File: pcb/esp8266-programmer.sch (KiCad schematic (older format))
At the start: 20 parts, among them P1 USB_OTG, P2 CONN_01X04, P3 CONN_01X05, P4 CONN_01X05, SW1 RESET, SW2 FLASH, SW3 SW_DP3T, U1 MCP1700T-3302E/TT, U2 MCP2221-I/SL, U3 74LS125, U99 ESP-12

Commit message: Interim stage
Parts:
- removed P1: USB_OTG, symbol USB_OTG-RESCUE-esp8266-programmer
- removed P3, P4: CONN_01X05, symbol CONN_01X05
- removed U3: 74LS125, symbol 74LS125
- added P1: USB_OTG, ruriwo/KiCad_MicroUSB.pretty:ZX62R-B-5P, symbol USB_OTG
- added P3: CONN_02X05, madworm/DIL-Headers.pretty:DIL-5, symbol CONN_02X05
- added R5: 10K, KiCad/Resistors_SMD.pretty:R_1206_HandSoldering, symbol R
- C1, C2, C3: footprint (none) -> KiCad/Capacitors_ThroughHole.pretty:CP_Radial_D5.0mm_P2.50mm
- C4: footprint (none) -> KiCad/Capacitors_SMD.pretty:C_1206_HandSoldering
- JP1: footprint (none) -> madworm/SIL-Headers.pretty:SIL-3
- P2: footprint (none) -> madworm/SIL-Headers.pretty:SIL-5
- R1, R2, R3, R4: value R -> 10K; footprint (none) -> KiCad/Resistors_SMD.pretty:R_1206_HandSoldering
- SW1, SW2: footprint (none) -> KiCad/Buttons_Switches_ThroughHole.pretty:SW_PUSH_6mm_h4.3mm
- SW3: footprint (none) -> KiCad/Buttons_Switches_ThroughHole.pretty:SW_DIP_x3_W7.62mm_Slide_LowProfile
- U2: footprint IPC7351-Nominal:SOIC127P600X175-14 -> KiCad/Housings_SOIC.pretty:SOIC-14_3.9x8.7mm_Pitch1.27mm
- U99: footprint jdunmire/kicad-ESP8266/ESP8266.pretty:ESP-12 -> bgowland/esp12-pogo_pins:ESP-12-with-pogo-pin-pads
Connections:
- net D+: now also P1.3 (D+)
- net D-: now also P1.2 (D-)
- net GND: now also P1.5 (GND), P1.6 (shield), R5.2; no longer C2.1, C3.1, R1.1, R2.1, R3.1, R4.1, SW3.1, SW3.6 (ComB), U2.1 (V+), U99.10 (GPIO15), U99.8 (VCC)
- net PP_ADC: now also P3.1 (P1)
- net PP_GPIO0: now also P3.6 (P6)
- net PP_GPIO12: now also P3.7 (P7)
- net PP_GPIO13: now also P3.9 (P9)
- net PP_GPIO14: now also P3.5 (P5)
- net PP_GPIO16: now also P3.3 (P3)
- net PP_GPIO2: now also P3.8 (P8)
- net PP_GPIO4: now also P3.4 (P4)
- net PP_GPIO5: now also P3.2 (P2)
- new net PP_GPIO15: P3.10 (P10), R5.1, U99.10 (GPIO15)
- new net VBUS: C3.1, P1.1 (VBUS), SW3.1, U2.1 (V+)
- new net VCC: C2.1, R1.1, R2.1, R3.1, R4.1, SW3.6 (ComB), U99.8 (VCC)
- no-connect marks 8 -> 11
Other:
- moved on the sheet: C3, R2

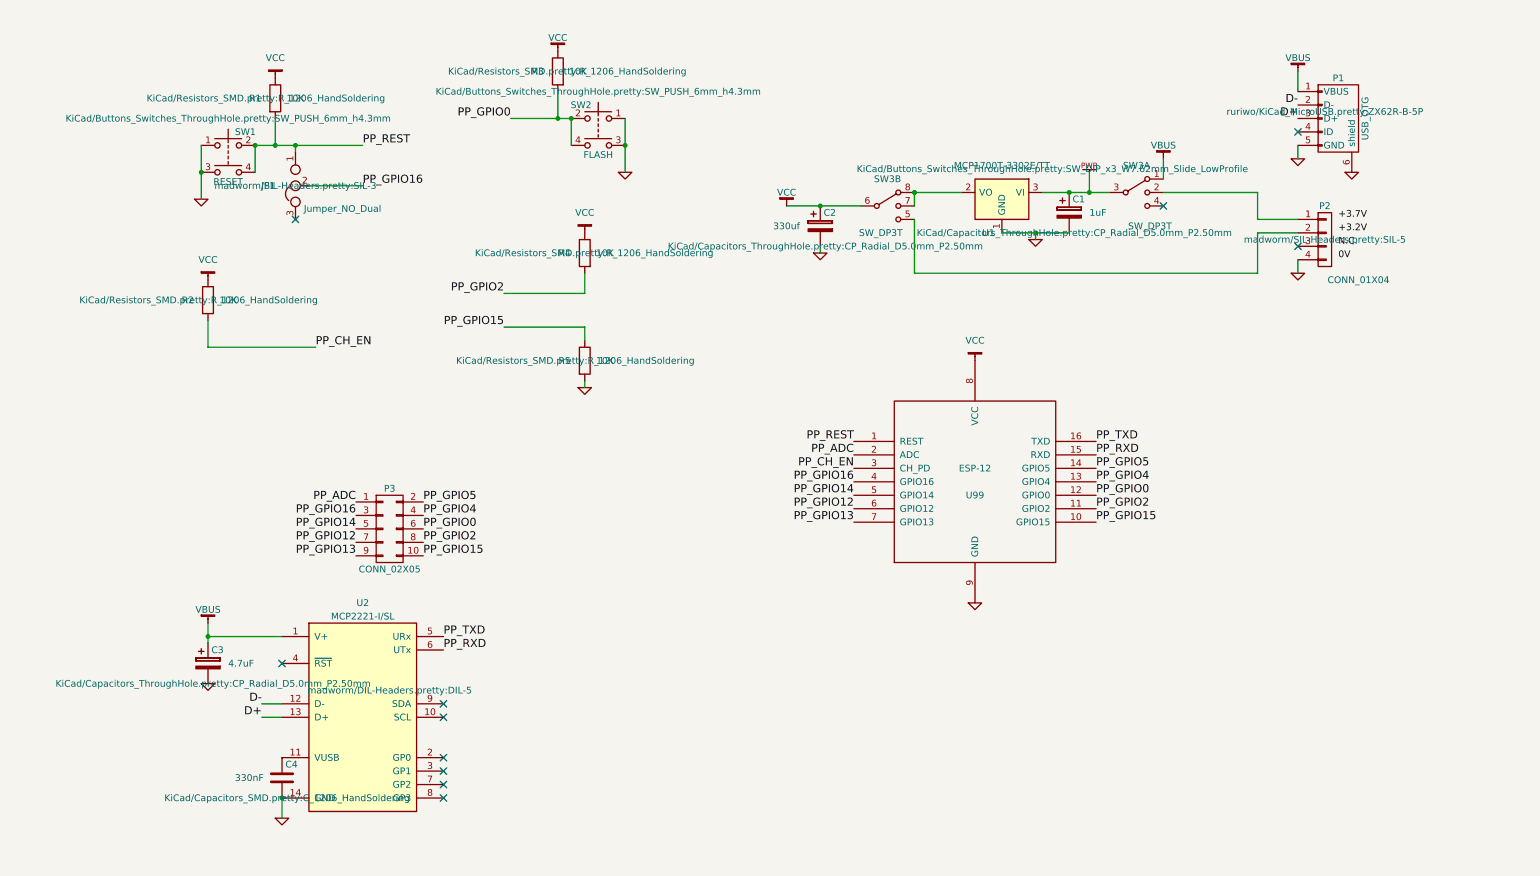
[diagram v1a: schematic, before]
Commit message: Add CH340G and new reset/flash circuit
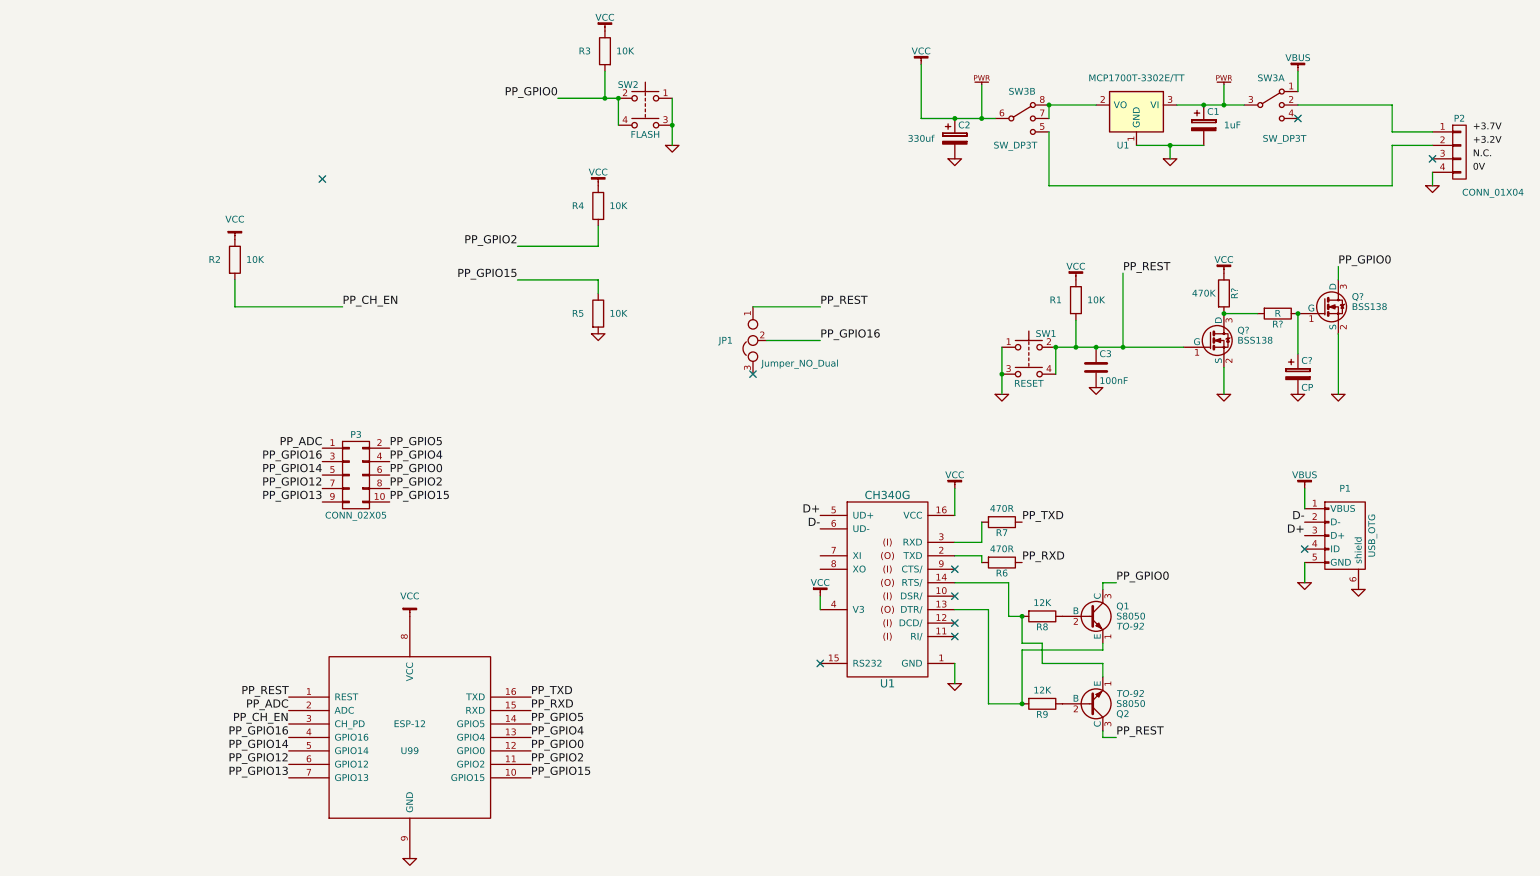
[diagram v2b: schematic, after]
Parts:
- removed C3: 4.7uF, KiCad/Capacitors_ThroughHole.pretty:CP_Radial_D5.0mm_P2.50mm, symbol CP
- removed C4: 330nF, KiCad/Capacitors_SMD.pretty:C_1206_HandSoldering, symbol C
- removed U2: MCP2221-I/SL, KiCad/Housings_SOIC.pretty:SOIC-14_3.9x8.7mm_Pitch1.27mm, symbol MCP2221-I/SL
- added C3: 100nF, symbol C
- added C?: CP, symbol CP
- added Q1, Q2: S8050, TO-92, symbol S8050
- added Q? (x2): BSS138, TO_SOT_Packages_SMD:SOT-23, symbol BSS138
- added R6, R7: 470R, symbol R
- added R8, R9: 12K, symbol R
- added R?: 470K, symbol R
- added R?: R, symbol R
- added U1: CH340G, symbol CH340G
- P1: footprint ruriwo/KiCad_MicroUSB.pretty:ZX62R-B-5P -> greatscottgadgets/gsg-kicad-lib/gsg-modules.pretty:USB-MICROB-FCI-10103592-LONGPADS
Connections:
- net D+: now also U1.5 (UD+)
- net D-: now also U1.6 (UD-)
- net GND: now also C3.2, C?.2, Q?.2 (S), Q?.2 (S), U1.1 (GND)
- net PP_GPIO0: now also Q1.3 (C), Q?.3 (D)
- net PP_REST: now also C3.1, Q2.3 (C), Q?.1 (G)
- net PP_RXD: now also R6.1
- net PP_TXD: now also R7.1
- net VCC: now also R?.1, U1.16 (VCC), U1.4 (V3)
- new net: Q1.1 (E), R9.2, U1.13 (DTR/)
- new net: Q2.1 (E), R8.2, U1.14 (RTS/)
- new net: R6.2, U1.2 (TXD)
- new net: R7.2, U1.3 (RXD)
- new net: Q1.2 (B), R8.1
- new net: Q2.2 (B), R9.1
- new net: C?.1, Q?.1 (G), R?.1
- new net: Q?.3 (D), R?.2, R?.2
- no-connect marks 11 -> 10
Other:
- moved on the sheet: C1, C2, JP1, P2, P3, R1, R2, R3, R4, R5, SW1, SW2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

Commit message: Add final components for CH230G & RST/FLA switch
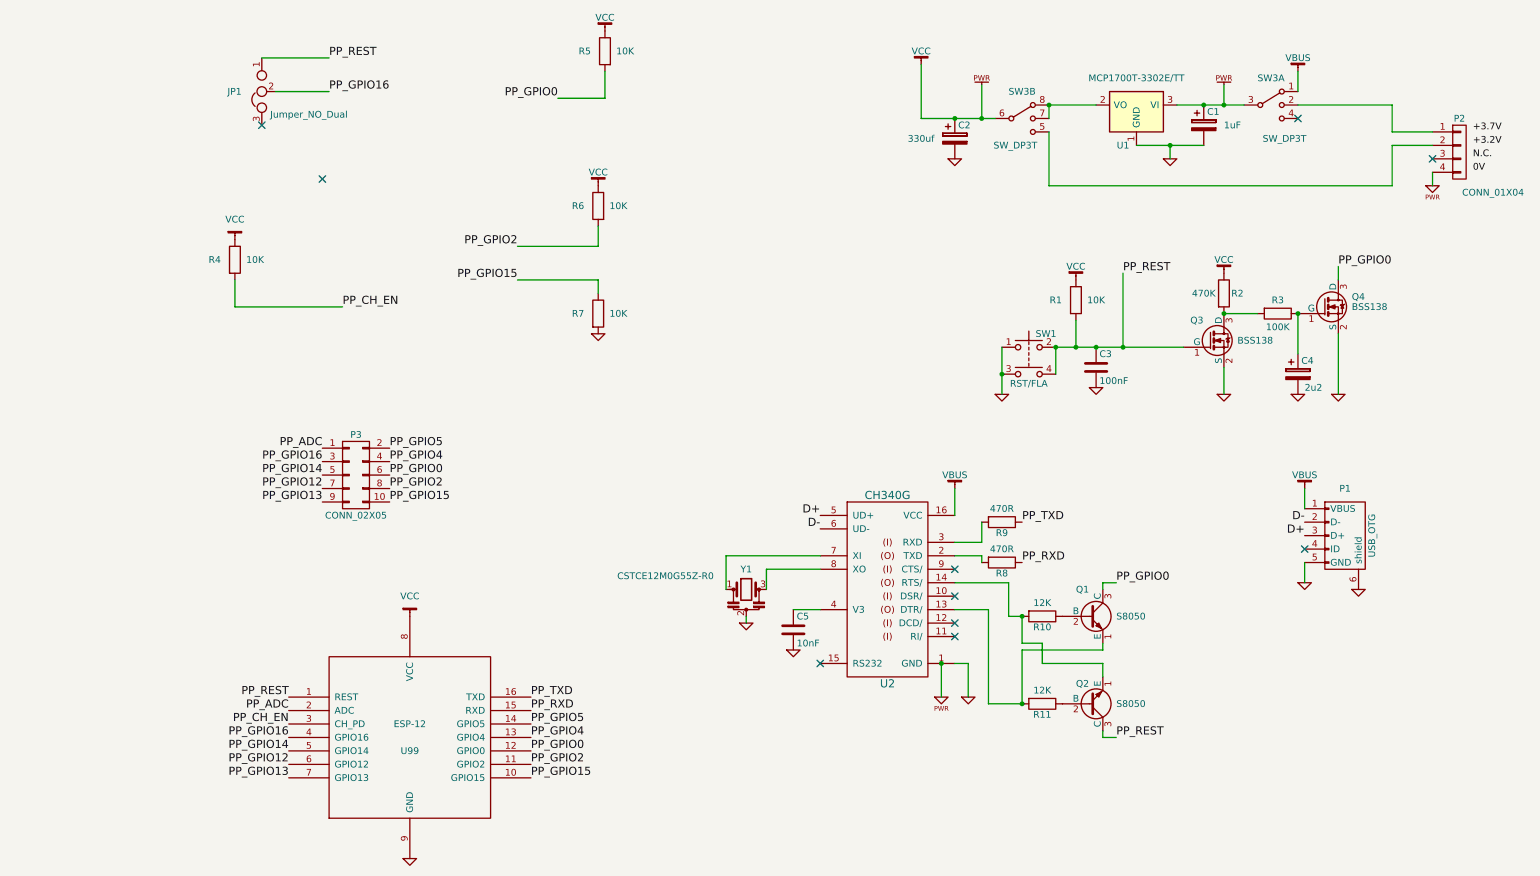
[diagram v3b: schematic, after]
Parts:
- removed SW2: FLASH, KiCad/Buttons_Switches_ThroughHole.pretty:SW_PUSH_6mm_h4.3mm, symbol SW_Push_Dual
- added C5: 10nF, symbol C
- added Y1: CSTCE12M0G55Z-R0, symbol Resonator
- C4: renamed from C?; value CP -> 2u2
- Q1, Q2: footprint TO-92 -> SOT-23
- R3: renamed from R?; value R -> 100K
- SW1: value RESET -> RST/FLA
- gave numbers to parts that had none: 3
- renumbered R8 to R10, R9 to R11, R2 to R4, R3 to R5, R4 to R6, R5 to R7, R6 to R8, R7 to R9, U1 to U2
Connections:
- net GND: now also C5.2, Y1.2; no longer P2.4 (P4)
- net VBUS: now also U2.16 (VCC)
- net VCC: no longer U2.16 (VCC), U2.4 (V3)
- net at U2.7 (XI): now also Y1.1
- net at U2.8 (XO): now also Y1.3
- new net: C5.1, U2.4 (V3)
- new net PWRGND: P2.4 (P4)
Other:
- moved on the sheet: JP1
